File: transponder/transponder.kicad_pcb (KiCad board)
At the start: 2 copper layers, 15.6 x 12.4 mm, 7 parts, among them IC1 ATTINY45-S, P1 POWER_CONN, P2 CONN_01X05

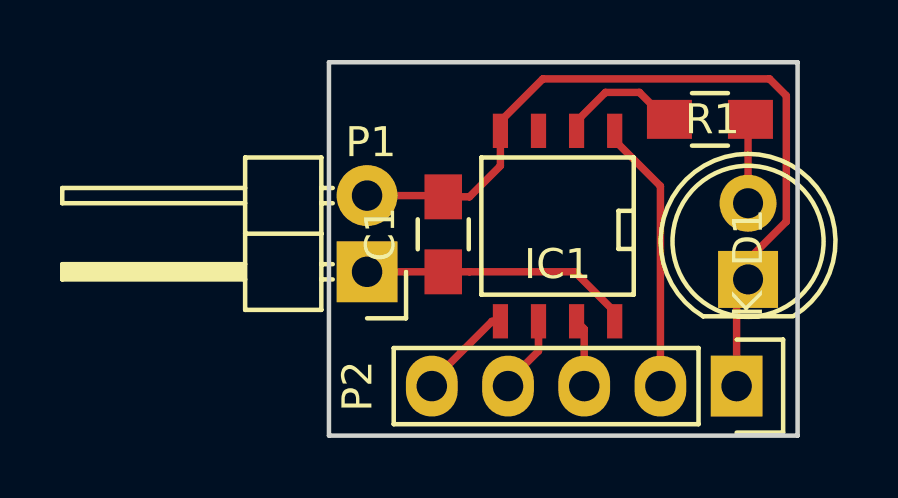
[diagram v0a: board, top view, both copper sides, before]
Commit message: transponder: Rewire LED
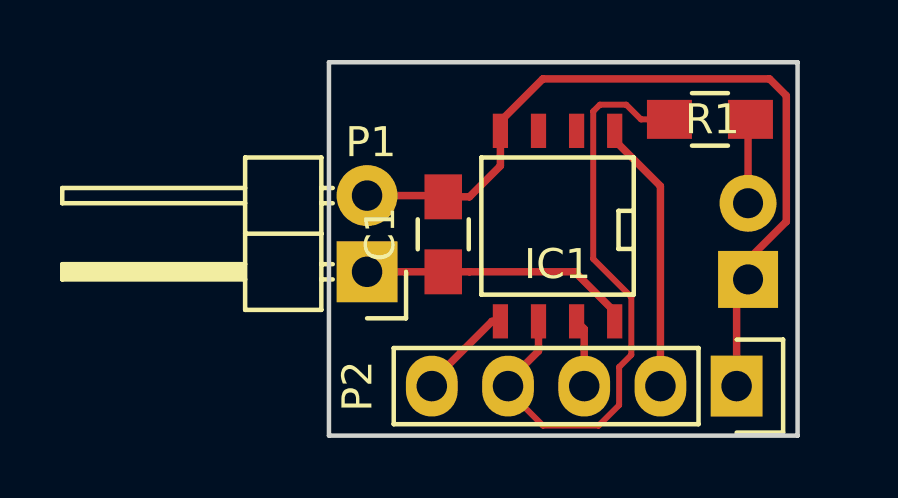
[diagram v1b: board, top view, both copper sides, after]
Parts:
- D1: moved to B.Cu
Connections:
- IC1 pad 2: Net-(IC1-Pad2) -> (no net)
- R1 pad 1: Net-(IC1-Pad2) -> /PROG_MISO
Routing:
- net /PROG_MISO: track 2.58 -> 20.6 mm
- net Net-(IC1-Pad2): track 4.72 -> 0.00 mm
- net (no net): track 0.00 -> 0.85 mm
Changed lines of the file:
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@@
     (thickness 1.6)
     (drawings 7)
-    (tracks 48)
+    (tracks 58)
     (zones 0)
     (modules 7)
-    (nets 9)
+    (nets 8)
   )
   (page A4)
@@
   )
   (setup
-    (last_trace_width 0.25)
+    (last_trace_width 0.2)
     (user_trace_width 0.2)
     (user_trace_width 0.5)
@@
   (net 5 /PROG_MISO)
   (net 6 /PROG_MOSI)
-  (net 7 "Net-(IC1-Pad2)")
-  (net 8 /PROG_RESET)
+  (net 7 /PROG_RESET)
   (net_class Default "To jest domyślna klasa połączeń."
     (clearance 0.2)
@@
     (add_net GND)
     (add_net "Net-(D1-Pad2)")
-    (add_net "Net-(IC1-Pad2)")
     (add_net VCC)
   )
@@
     )
   )
-  (module LEDs:LED-5MM (layer F.Cu)
+  (module LEDs:LED-5MM (layer B.Cu)
     (at 138.43 96.774 90)
     (descr "LED 5mm round vertical")
     (tags "LED 5mm round vertical")
-    (fp_text reference D1 (at 1.397 0 90) (layer F.SilkS)
-      (effects (font (size 1 1) (thickness 0.15)))
-    )
-    (fp_text value IR_LED (at 1.524 -2.54 90) (layer F.Fab)
-      (effects (font (size 1 1) (thickness 0.15)))
-    )
-    (fp_line (start -1.5 -1.55) (end -1.5 1.55) (layer F.CrtYd) (width 0.05))
-    (fp_arc (start 1.3 0) (end -1.5 1.55) (angle -302) (layer F.CrtYd) (width 0.05))
-    (fp_arc (start 1.27 0) (end -1.23 -1.5) (angle 297.5) (layer F.SilkS) (width 0.15))
-    (fp_line (start -1.23 1.5) (end -1.23 -1.5) (layer F.SilkS) (width 0.15))
-    (fp_circle (center 1.27 0) (end 0.97 -2.5) (layer F.SilkS) (width 0.15))
-    (fp_text user K (at -0.8255 0 90) (layer F.SilkS)
-      (effects (font (size 1 1) (thickness 0.15)))
-    )
-    (pad 1 thru_hole rect (at 0 0 180) (size 2 1.9) (drill 1.00076) (layers *.Cu *.Mask F.SilkS)
+    (fp_text reference D1 (at 1.397 0 90) (layer B.SilkS)
+      (effects (font (size 1 1) (thickness 0.15)) (justify mirror))
+    )
+    (fp_text value IR_LED (at 1.524 2.54 90) (layer B.Fab)
+      (effects (font (size 1 1) (thickness 0.15)) (justify mirror))
+    )
+    (fp_line (start -1.5 1.55) (end -1.5 -1.55) (layer B.CrtYd) (width 0.05))
+    (fp_arc (start 1.3 0) (end -1.5 -1.55) (angle 302) (layer B.CrtYd) (width 0.05))
+    (fp_arc (start 1.27 0) (end -1.23 1.5) (angle -297.5) (layer B.SilkS) (width 0.15))
+    (fp_line (start -1.23 -1.5) (end -1.23 1.5) (layer B.SilkS) (width 0.15))
+    (fp_circle (center 1.27 0) (end 0.97 2.5) (layer B.SilkS) (width 0.15))
+    (fp_text user K (at -0.8255 0 90) (layer B.SilkS)
+      (effects (font (size 1 1) (thickness 0.15)) (justify mirror))
+    )
+    (pad 1 thru_hole rect (at 0 0) (size 2 1.9) (drill 1.00076) (layers *.Cu *.Mask B.SilkS)
       (net 2 GND))
-    (pad 2 thru_hole circle (at 2.54 0 90) (size 1.9 1.9) (drill 1.00076) (layers *.Cu *.Mask F.SilkS)
+    (pad 2 thru_hole circle (at 2.54 0 90) (size 1.9 1.9) (drill 1.00076) (layers *.Cu *.Mask B.SilkS)
       (net 3 "Net-(D1-Pad2)"))
     (model LEDs.3dshapes/LED-5MM.wrl
@@
       (net 2 GND))
     (pad 3 smd rect (at 0.635 3.175 180) (size 0.508 1.143) (layers F.Cu F.Paste F.Mask))
-    (pad 2 smd rect (at -0.635 3.175 180) (size 0.508 1.143) (layers F.Cu F.Paste F.Mask)
-      (net 7 "Net-(IC1-Pad2)"))
+    (pad 2 smd rect (at -0.635 3.175 180) (size 0.508 1.143) (layers F.Cu F.Paste F.Mask))
     (pad 1 smd rect (at -1.905 3.175 180) (size 0.508 1.143) (layers F.Cu F.Paste F.Mask)
-      (net 8 /PROG_RESET))
+      (net 7 /PROG_RESET))
     (model SMD_Packages.3dshapes/SOIC-8-N.wrl
       (at (xyz 0 0 0))
@@
       (net 2 GND))
     (model Pin_Headers.3dshapes/Pin_Header_Angled_1x02.wrl
-      (at (xyz 0 -0.05 0))
+      (at (xyz 0 -0.05 -1))
       (scale (xyz 1 1 1))
-      (rotate (xyz 0 0 90))
+      (rotate (xyz 0 180 90))
     )
   )
@@
     (fp_line (start -0.6 -0.875) (end 0.6 -0.875) (layer F.SilkS) (width 0.15))
     (pad 1 smd rect (at -1.35 0) (size 1.5 1.3) (layers F.Cu F.Paste F.Mask)
-      (net 7 "Net-(IC1-Pad2)"))
+      (net 5 /PROG_MISO))
     (pad 2 smd rect (at 1.35 0) (size 1.5 1.3) (layers F.Cu F.Paste F.Mask)
       (net 3 "Net-(D1-Pad2)"))
@@
       (net 2 GND))
     (pad 2 thru_hole oval (at 0 2.54 270) (size 2.032 1.7272) (drill 1.016) (layers *.Cu *.Mask F.SilkS)
-      (net 8 /PROG_RESET))
+      (net 7 /PROG_RESET))
     (pad 3 thru_hole oval (at 0 5.08 270) (size 2.032 1.7272) (drill 1.016) (layers *.Cu *.Mask F.SilkS)
       (net 4 /PROG_SCK))
@@
   (gr_line (start 140.081 89.535) (end 140.081 101.981) (layer Edge.Cuts) (width 0.15))
   (gr_line (start 124.46 89.535) (end 140.081 89.535) (layer Edge.Cuts) (width 0.15))
+  (segment (start 132.715 91.821) (end 132.715 91.5035) (width 0.25) (layer F.Cu) (net 0))
+  (segment (start 132.715 91.44) (end 132.715 91.975) (width 0.25) (layer F.Cu) (net 0))
   (segment (start 133.985 98.171) (end 133.985 97.8535) (width 0.25) (layer F.Cu) (net 1))
   (segment (start 133.985 97.8535) (end 132.6515 96.52) (width 0.25) (layer F.Cu) (net 1))
-  (segment (start 132.6515 96.52) (end 129.145 96.52) (width 0.25) (layer F.Cu) (net 1))
   (segment (start 129.145 96.52) (end 128.27 96.52) (width 0.25) (layer F.Cu) (net 1))
   (segment (start 125.73 96.52) (end 128.27 96.52) (width 0.25) (layer F.Cu) (net 1))
+  (segment (start 132.6515 96.52) (end 129.145 96.52) (width 0.25) (layer F.Cu) (net 1))
   (segment (start 128.27 94.02) (end 129.145 94.02) (width 0.25) (layer F.Cu) (net 2))
   (segment (start 129.145 94.02) (end 130.175 92.99) (width 0.25) (layer F.Cu) (net 2))
@@
   (segment (start 132.969 100.33) (end 132.969 98.425) (width 0.25) (layer F.Cu) (net 4))
   (segment (start 132.969 98.425) (end 132.715 98.171) (width 0.25) (layer F.Cu) (net 4))
+  (segment (start 135.81 91.44) (end 134.86 91.44) (width 0.2) (layer F.Cu) (net 5))
+  (segment (start 133.269001 91.171497) (end 133.269001 96.089499) (width 0.2) (layer F.Cu) (net 5))
+  (segment (start 130.429 100.4824) (end 130.429 100.33) (width 0.2) (layer F.Cu) (net 5))
+  (segment (start 134.86 91.44) (end 134.369499 90.949499) (width 0.2) (layer F.Cu) (net 5))
+  (segment (start 134.539001 99.289226) (end 134.13261 99.695617) (width 0.2) (layer F.Cu) (net 5))
+  (segment (start 134.369499 90.949499) (end 133.490999 90.949499) (width 0.2) (layer F.Cu) (net 5))
+  (segment (start 133.490999 90.949499) (end 133.269001 91.171497) (width 0.2) (layer F.Cu) (net 5))
+  (segment (start 133.269001 96.089499) (end 134.539001 97.359499) (width 0.2) (layer F.Cu) (net 5))
+  (segment (start 134.539001 97.359499) (end 134.539001 99.289226) (width 0.2) (layer F.Cu) (net 5))
+  (segment (start 134.13261 99.695617) (end 134.13261 100.964383) (width 0.2) (layer F.Cu) (net 5))
+  (segment (start 134.13261 100.964383) (end 133.450983 101.64601) (width 0.2) (layer F.Cu) (net 5))
+  (segment (start 133.450983 101.64601) (end 131.59261 101.64601) (width 0.2) (layer F.Cu) (net 5))
+  (segment (start 131.59261 101.64601) (end 130.429 100.4824) (width 0.2) (layer F.Cu) (net 5))
   (segment (start 130.429 100.33) (end 130.429 100.1776) (width 0.25) (layer F.Cu) (net 5))
   (segment (start 131.445 99.1616) (end 131.445 98.9925) (width 0.25) (layer F.Cu) (net 5))
   (segment (start 130.429 100.1776) (end 131.445 99.1616) (width 0.25) (layer F.Cu) (net 5))
   (segment (start 131.445 98.9925) (end 131.445 98.171) (width 0.25) (layer F.Cu) (net 5))
+  (segment (start 135.71 91.44) (end 135.81 91.44) (width 0.25) (layer F.Cu) (net 5))
   (segment (start 127.889 100.33) (end 127.889 100.1776) (width 0.25) (layer F.Cu) (net 6))
   (segment (start 127.889 100.1776) (end 129.8956 98.171) (width 0.25) (layer F.Cu) (net 6))
@@
   (segment (start 128.27 100.33) (end 128.27 100.1776) (width 0.25) (layer F.Cu) (net 6))
   (segment (start 130.175 98.2726) (end 130.175 97.79) (width 0.25) (layer F.Cu) (net 6))
-  (segment (start 132.715 91.821) (end 132.715 91.5035) (width 0.25) (layer F.Cu) (net 7))
-  (segment (start 132.715 91.5035) (end 133.6785 90.54) (width 0.25) (layer F.Cu) (net 7))
-  (segment (start 133.6785 90.54) (end 134.81 90.54) (width 0.25) (layer F.Cu) (net 7))
-  (segment (start 134.81 90.54) (end 135.71 91.44) (width 0.25) (layer F.Cu) (net 7))
-  (segment (start 135.71 91.44) (end 135.81 91.44) (width 0.25) (layer F.Cu) (net 7))
-  (segment (start 132.715 91.44) (end 132.715 91.975) (width 0.25) (layer F.Cu) (net 7))
-  (segment (start 133.985 91.821) (end 133.985 92.1385) (width 0.25) (layer F.Cu) (net 8))
-  (segment (start 133.985 92.1385) (end 135.509 93.6625) (width 0.25) (layer F.Cu) (net 8))
-  (segment (start 135.509 93.6625) (end 135.509 99.064) (width 0.25) (layer F.Cu) (net 8))
-  (segment (start 135.509 99.064) (end 135.509 100.33) (width 0.25) (layer F.Cu) (net 8))
-  (segment (start 133.985 92.2615) (end 133.985 91.44) (width 0.25) (layer F.Cu) (net 8))
-  (segment (start 135.89 100.33) (end 135.89 100.254602) (width 0.25) (layer F.Cu) (net 8))
+  (segment (start 133.985 91.821) (end 133.985 92.1385) (width 0.25) (layer F.Cu) (net 7))
+  (segment (start 133.985 92.1385) (end 135.509 93.6625) (width 0.25) (layer F.Cu) (net 7))
+  (segment (start 135.509 93.6625) (end 135.509 99.064) (width 0.25) (layer F.Cu) (net 7))
+  (segment (start 135.509 99.064) (end 135.509 100.33) (width 0.25) (layer F.Cu) (net 7))
+  (segment (start 133.985 92.2615) (end 133.985 91.44) (width 0.25) (layer F.Cu) (net 7))
+  (segment (start 135.89 100.33) (end 135.89 100.254602) (width 0.25) (layer F.Cu) (net 7))
   (zone (net 2) (net_name GND) (layer F.Cu) (hatch edge 0.508)
     (connect_pads yes (clearance 0.508))
